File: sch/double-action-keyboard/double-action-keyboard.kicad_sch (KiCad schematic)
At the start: 5 parts, among them U1 Pico

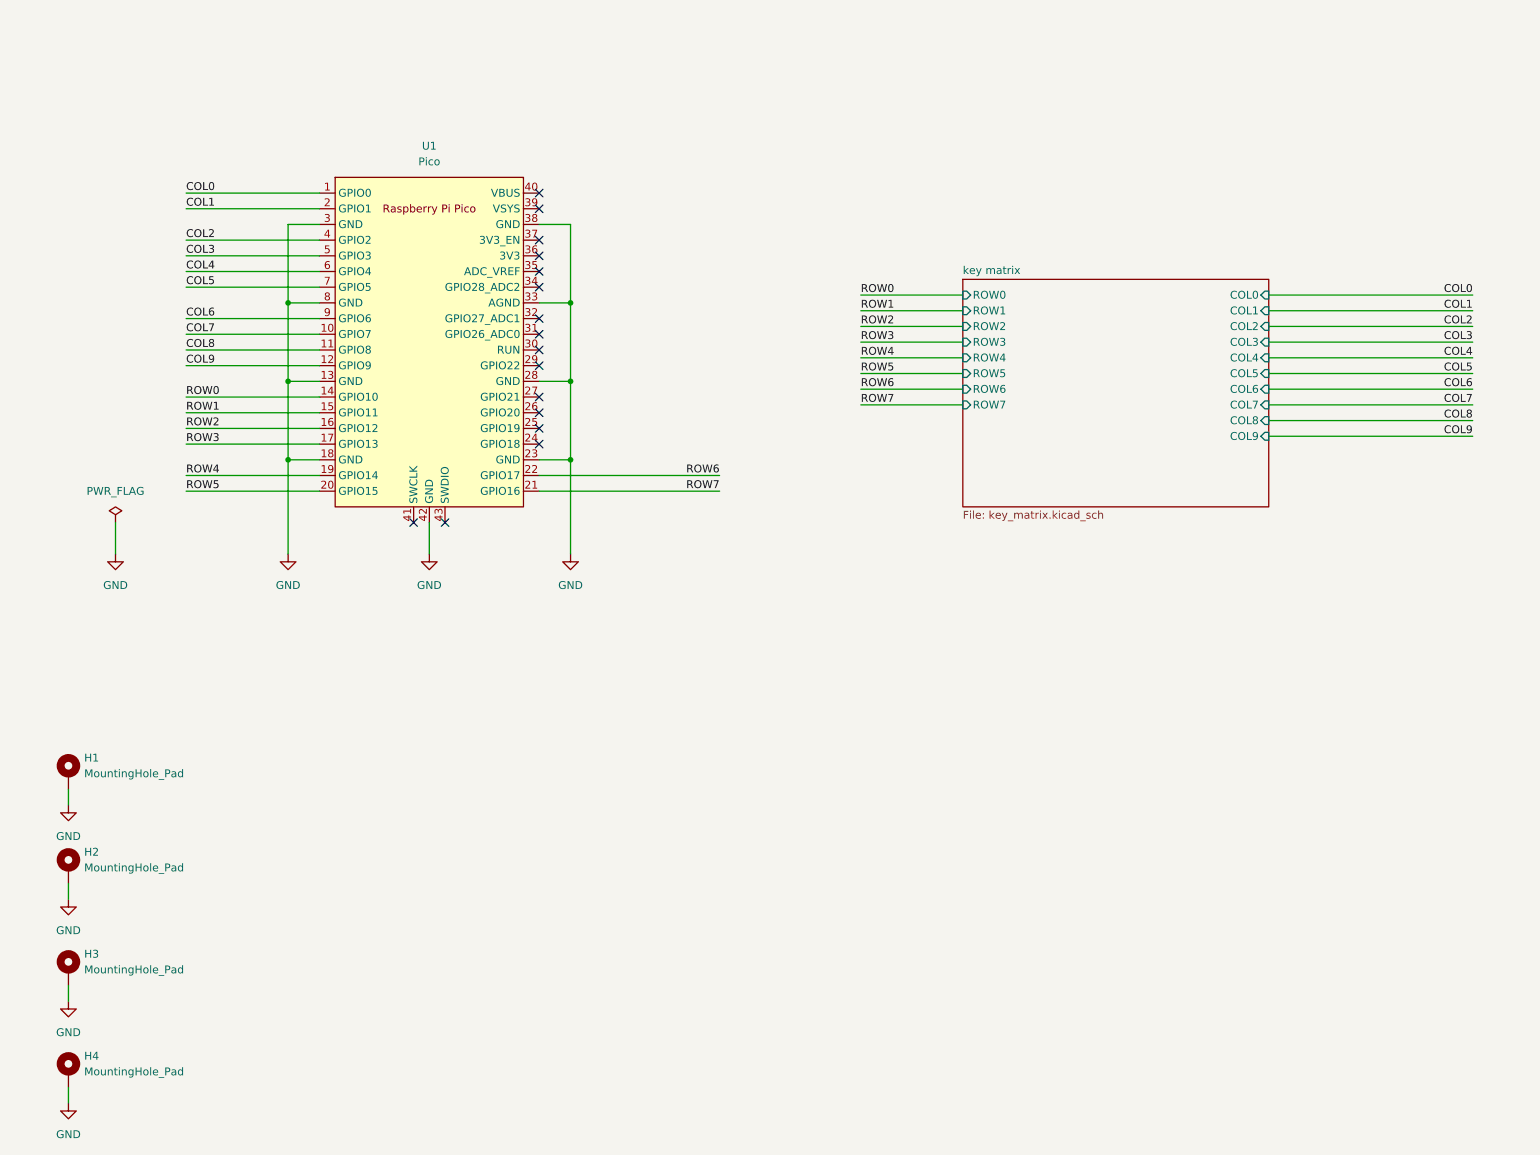
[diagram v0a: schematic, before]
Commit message: ダイオードの配置と配線を行いました。
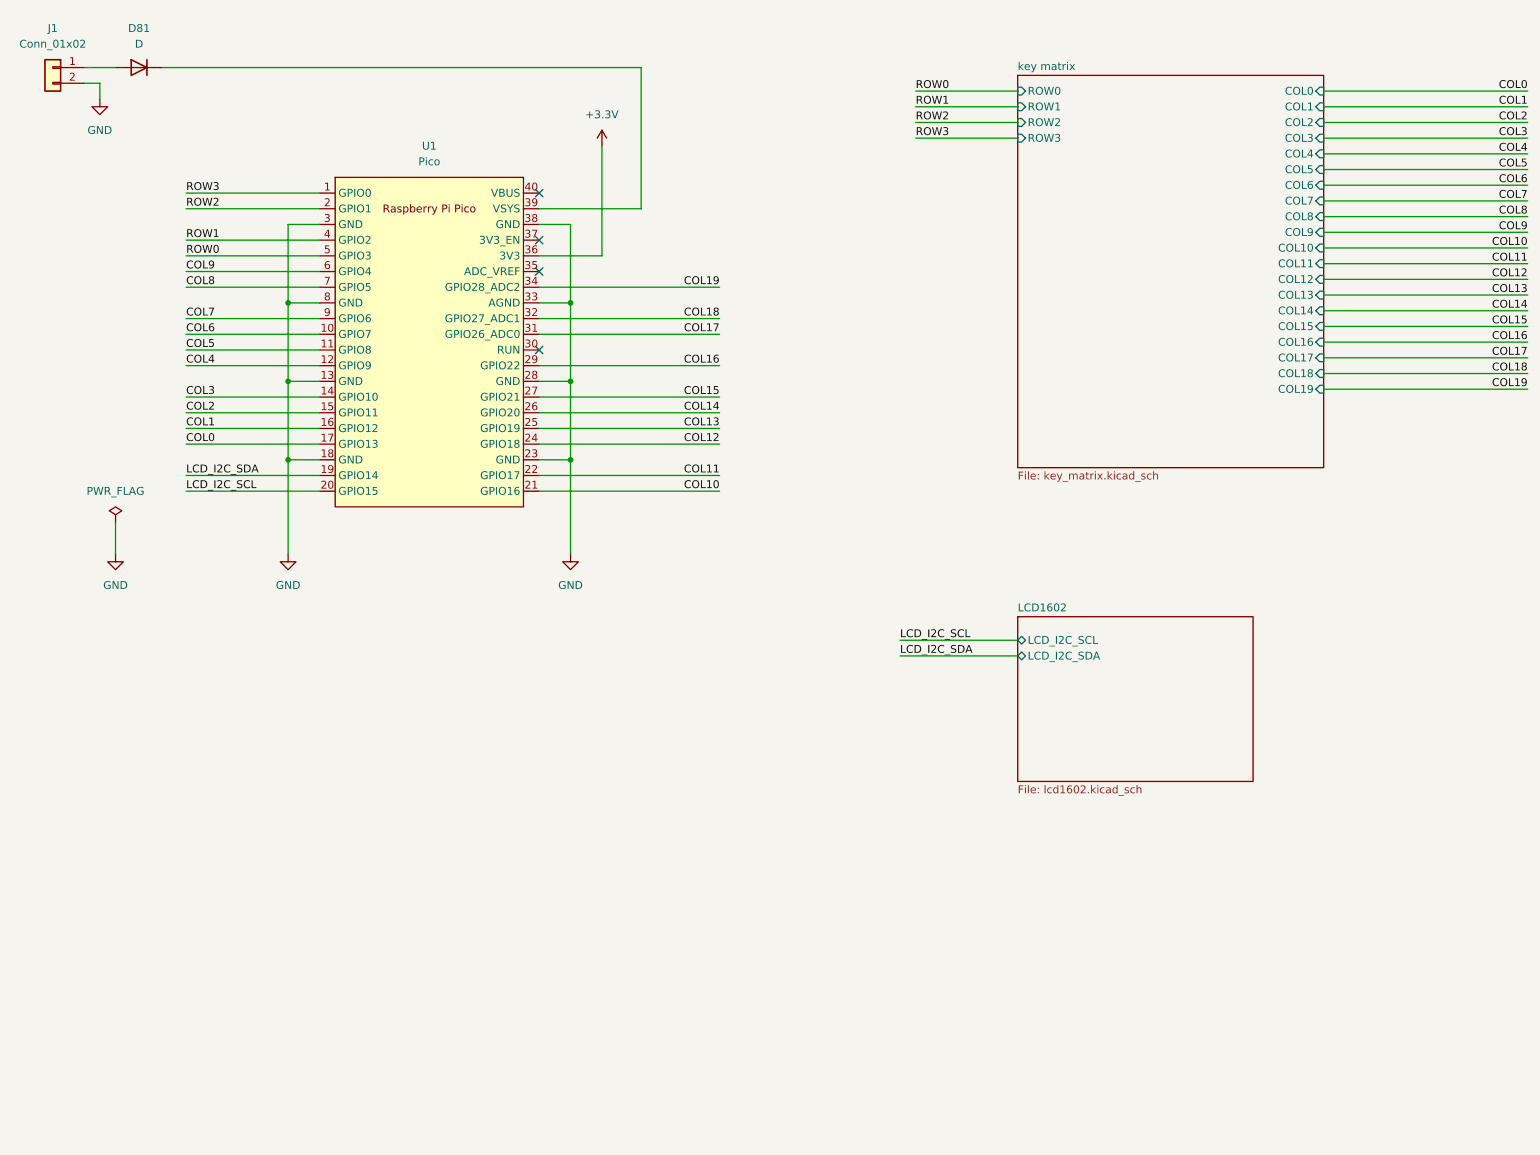
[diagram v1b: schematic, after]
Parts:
- removed H1, H2, H3, H4: MountingHole_Pad, MountingHole:MountingHole_3.2mm_M3_Pad, symbol Mechanical:MountingHole_Pad
- removed U1: Pico, MCU_RaspberryPi_and_Boards:RPi_Pico_SMD_TH, symbol pico:Pico
- added D81: D, Diode_SMD:D_SOD-123, symbol Device:D
- added J1: Conn_01x02, Connector_JST:JST_XH_B2B-XH-A_1x02_P2.50mm_Vertical, symbol Connector_Generic:Conn_01x02
- added U1: Pico, my_pico_smd:pico_no_dbg_smd_th, symbol my_pico:my_pico_no_dbg
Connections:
- net COL0: now also U1.17 (GPIO13)
- net COL1: now also U1.16 (GPIO12)
- net COL2: now also U1.15 (GPIO11)
- net COL3: now also U1.14 (GPIO10)
- net COL4: now also U1.12 (GPIO9)
- net COL5: now also U1.11 (GPIO8)
- net COL6: now also U1.10 (GPIO7)
- net COL7: now also U1.9 (GPIO6)
- net COL8: now also U1.7 (GPIO5)
- net COL9: now also U1.6 (GPIO4)
- net GND: now also J1.2 (Pin_2), U1.13 (GND), U1.18 (GND), U1.23 (GND), U1.28 (GND), U1.3 (GND), U1.33 (AGND), U1.38 (GND), U1.8 (GND)
- net ROW0: now also U1.5 (GPIO3)
- net ROW1: now also U1.4 (GPIO2)
- net ROW2: now also U1.2 (GPIO1)
- net ROW3: now also U1.1 (GPIO0)
- new net: D81.1 (K), U1.39 (VSYS)
- new net: D81.2 (A), J1.1 (Pin_1)
- new net +3.3V: U1.36 (3V3)
- new net COL10: U1.21 (GPIO16)
- new net COL11: U1.22 (GPIO17)
- new net COL12: U1.24 (GPIO18)
- new net COL13: U1.25 (GPIO19)
- new net COL14: U1.26 (GPIO20)
- new net COL15: U1.27 (GPIO21)
- new net COL16: U1.29 (GPIO22)
- new net COL17: U1.31 (GPIO26_ADC0)
- new net COL18: U1.32 (GPIO27_ADC1)
- new net COL19: U1.34 (GPIO28_ADC2)
- new net LCD_I2C_SCL: U1.20 (GPIO15)
- new net LCD_I2C_SDA: U1.19 (GPIO14)
- no-connect marks 16 -> 4
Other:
- added sheet LCD1602 (lcd1602.kicad_sch)
- sheet key matrix ports: added COL10, COL11, COL12, COL13, COL14, COL15, COL16, COL17, COL18, COL19; removed ROW4, ROW5, ROW6, ROW7

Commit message: KiCad 8.0にアップデートしました。 部品配置をやり直し中。
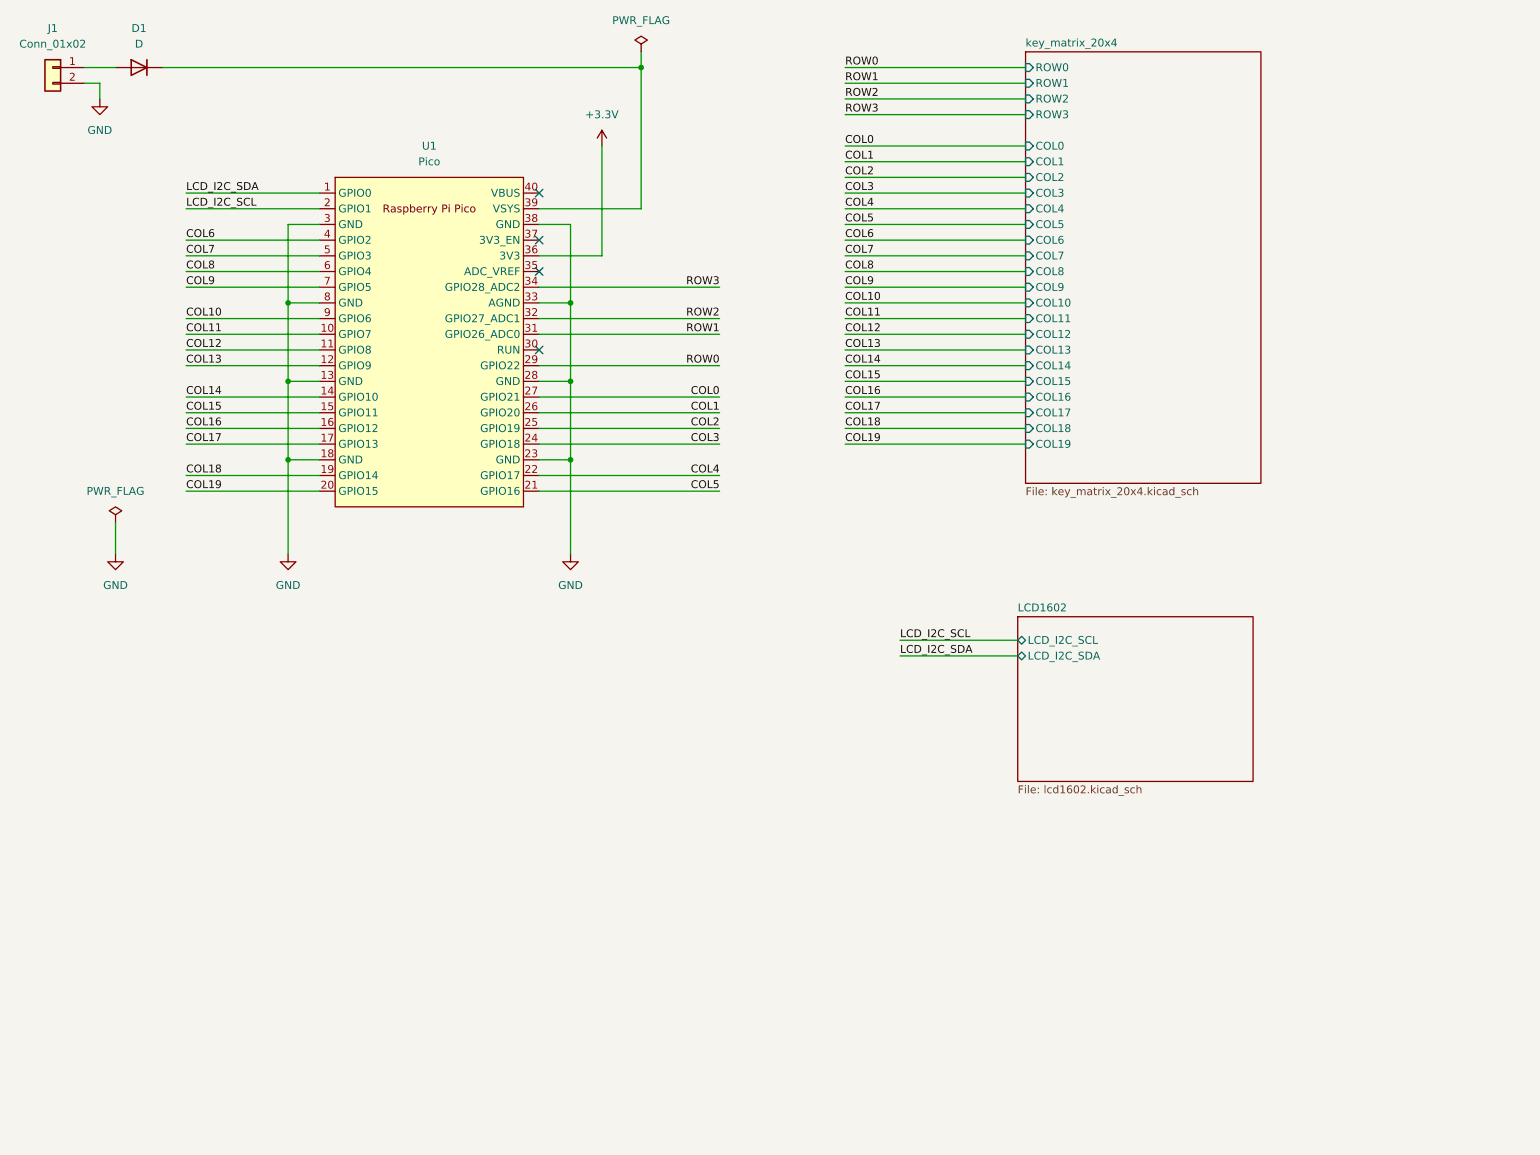
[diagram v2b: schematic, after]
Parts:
- J1: footprint Connector_JST:JST_XH_B2B-XH-A_1x02_P2.50mm_Vertical -> Connector_JST:JST_PH_B2B-PH-K_1x02_P2.00mm_Vertical
- renumbered D81 to D1
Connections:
- net COL0: now also U1.27 (GPIO21); no longer U1.17 (GPIO13)
- net COL1: now also U1.26 (GPIO20); no longer U1.16 (GPIO12)
- net COL10: now also U1.9 (GPIO6); no longer U1.21 (GPIO16)
- net COL11: now also U1.10 (GPIO7); no longer U1.22 (GPIO17)
- net COL12: now also U1.11 (GPIO8); no longer U1.24 (GPIO18)
- net COL13: now also U1.12 (GPIO9); no longer U1.25 (GPIO19)
- net COL14: now also U1.14 (GPIO10); no longer U1.26 (GPIO20)
- net COL15: now also U1.15 (GPIO11); no longer U1.27 (GPIO21)
- net COL16: now also U1.16 (GPIO12); no longer U1.29 (GPIO22)
- net COL17: now also U1.17 (GPIO13); no longer U1.31 (GPIO26_ADC0)
- net COL18: now also U1.19 (GPIO14); no longer U1.32 (GPIO27_ADC1)
- net COL19: now also U1.20 (GPIO15); no longer U1.34 (GPIO28_ADC2)
- net COL2: now also U1.25 (GPIO19); no longer U1.15 (GPIO11)
- net COL3: now also U1.24 (GPIO18); no longer U1.14 (GPIO10)
- net COL4: now also U1.22 (GPIO17); no longer U1.12 (GPIO9)
- net COL5: now also U1.21 (GPIO16); no longer U1.11 (GPIO8)
- net COL6: now also U1.4 (GPIO2); no longer U1.10 (GPIO7)
- net COL7: now also U1.5 (GPIO3); no longer U1.9 (GPIO6)
- net COL8: now also U1.6 (GPIO4); no longer U1.7 (GPIO5)
- net COL9: now also U1.7 (GPIO5); no longer U1.6 (GPIO4)
- net LCD_I2C_SCL: now also U1.2 (GPIO1); no longer U1.20 (GPIO15)
- net LCD_I2C_SDA: now also U1.1 (GPIO0); no longer U1.19 (GPIO14)
- net ROW0: now also U1.29 (GPIO22); no longer U1.5 (GPIO3)
- net ROW1: now also U1.31 (GPIO26_ADC0); no longer U1.4 (GPIO2)
- net ROW2: now also U1.32 (GPIO27_ADC1); no longer U1.2 (GPIO1)
- net ROW3: now also U1.34 (GPIO28_ADC2); no longer U1.1 (GPIO0)
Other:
- removed sheet key matrix
- added sheet key_matrix_20x4 (key_matrix_20x4.kicad_sch)

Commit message: ざっくり配線しました。 線間はもっと詰める予定。
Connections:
- net ROW0: now also U1.34 (GPIO28_ADC2); no longer U1.29 (GPIO22)
- net ROW1: now also U1.32 (GPIO27_ADC1); no longer U1.31 (GPIO26_ADC0)
- net ROW2: now also U1.31 (GPIO26_ADC0); no longer U1.32 (GPIO27_ADC1)
- net ROW3: now also U1.29 (GPIO22); no longer U1.34 (GPIO28_ADC2)
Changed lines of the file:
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@@
 	)
 	(label "ROW2"
-		(at 128.27 62.23 180)
+		(at 128.27 64.77 180)
 		(fields_autoplaced yes)
 		(effects
@@
 	)
 	(label "ROW1"
-		(at 128.27 64.77 180)
+		(at 128.27 62.23 180)
 		(fields_autoplaced yes)
 		(effects
@@
 	)
 	(label "ROW0"
-		(at 128.27 69.85 180)
+		(at 128.27 57.15 180)
 		(fields_autoplaced yes)
 		(effects
@@
 	)
 	(label "ROW3"
-		(at 128.27 57.15 180)
-		(fields_autoplaced yes)
-		(effects
+		(at 128.27 69.85 180)
+		(fields_autoplaced yes)
+		(effects
